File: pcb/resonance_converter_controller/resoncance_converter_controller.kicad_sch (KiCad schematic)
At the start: 53 parts, among them J2 USB_C_Receptacle_USB2.0_14P, J4 Conn_02x19_Odd_Even, J5 Conn_01x02, J6 FX18-120S-0.8SH, J7 Conn_ARM_SWD_TagConnect_TC2030, U22 USBLC6-2P6, U23 OPA356xxDBV, U24 AD5246BKSZ100-RL7

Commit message: Add io panel and fix controller pcb
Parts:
- added C101, C102: 100nF, Capacitor_SMD:C_0402_1005Metric, symbol Device:C
- added CN1: AXK5S40047YG, AXK5S40047YG:CONN-SMD_40P-P0.50_AXK5S40047YG, symbol AXK5S40047YG:AXK5S40047YG
- added J3: DF12NB_5.0_-20DP-0.5V_51_, DF12NB_5.0_-20DP-0.5V_51_:HRS_DF12NB_5.0_-20DP-0.5V_51_, symbol DF12NB_5.0_-20DP-0.5V_51_:DF12NB_5.0_-20DP-0.5V_51_
- added U25: TMUX1574RSV, Package_DFN_QFN:UQFN-16_1.8x2.6mm_P0.4mm, symbol Analog_Switch:TMUX1574RSV
- added U26: TMUX154ERSW, Package_DFN_QFN:UQFN-10_1.4x1.8mm_P0.4mm, symbol Analog_Switch:TMUX154ERSW
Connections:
- net ENCODER_CHA: now also U26.3 (A); no longer J6.80
- net ENCODER_CHB: now also U26.5 (B); no longer J6.19
- net GND: now also C101.2, C102.2, CN1.21, CN1.22, CN1.23, CN1.24, CN1.25, CN1.26, CN1.27, CN1.28, CN1.29, CN1.30, CN1.31, CN1.32, CN1.33, CN1.34, CN1.35, CN1.36, CN1.37, CN1.38, CN1.39, CN1.40, J3.16, J3.18, J3.20, U25.13 (~{EN}), U25.6 (GND), U26.4 (GND), U26.8 (~{EN}); no longer J4.13 (Pin_13), J6.60
- net HRTIM_EEV9: now also J3.5
- net INT_I2C_SCL: now also J3.8
- net INT_I2C_SDA: now also J3.10
- net LCD_DC: now also U25.5 (D2); no longer J6.20
- net LCD_MOSI: now also U25.7 (D3); no longer J6.90
- net LCD_SCK: now also U25.2 (D1); no longer J6.29
- net LCD_SS: now also U25.10 (D4); no longer J6.92
- net VCC: now also C101.1, C102.1, J3.2, U25.14 (VDD), U26.9 (VCC)
- net VOUT: now also CN1.10, CN1.12, CN1.14, CN1.16, CN1.18, CN1.2, CN1.20, CN1.4, CN1.6, CN1.8
- net VSYS: now also CN1.1, CN1.11, CN1.13, CN1.15, CN1.17, CN1.19, CN1.3, CN1.5, CN1.7, CN1.9
- net Controller/NRST renamed NRST
- net NRST: now also J3.1
- net Controller/SWCLK renamed SWCLK
- net SWCLK: now also J3.19
- net Controller/SWDIO renamed SWDIO
- net SWDIO: now also J3.17
- net Power supply/3.3VP renamed +3.3VP
- net +3.3VP: now also J3.4, J3.6
- new net AUX_ADC: J4.13 (Pin_13), J6.60
- new net KEY_INT: J3.3
- new net LOCAL_ENCODER: U26.10 (SEL)
- new net LOCAL_ENCODER_CHA: J3.14, U26.1 (A0)
- new net LOCAL_ENCODER_CHB: J3.15, U26.7 (B0)
- new net LOCAL_LCD: U25.15 (SEL)
- new net LOCAL_LCD_DC: J3.11, U25.3 (S2A)
- new net LOCAL_LCD_MOSI: J3.7, U25.9 (S3A)
- new net LOCAL_LCD_SCK: J3.13, U25.16 (S1A)
- new net LOCAL_LCD_SS: J3.9, U25.12 (S4A)
- new net REMOTE_ENCODER_CHA: J6.80, U26.2 (A1)
- new net REMOTE_ENCODER_CHB: J6.19, U26.6 (B1)
- new net REMOTE_LCD_DC: J6.20, U25.4 (S2B)
- new net REMOTE_LCD_MOSI: J6.90, U25.8 (S3B)
- new net REMOTE_LCD_SCK: J6.29, U25.1 (S1B)
- new net REMOTE_LCD_SS: J6.92, U25.11 (S4B)
- new net /QON: J3.12
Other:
- sheet Analog preprocess ports: added AUX_ADC, AUX_ADC_OUT; removed none
- sheet Controller ports: added AUX_ADC_OUT, KEY_INT, LCD_LOCAL, LOCAL_ENCODER; removed none
- sheet Power supply ports: added /QON; removed none

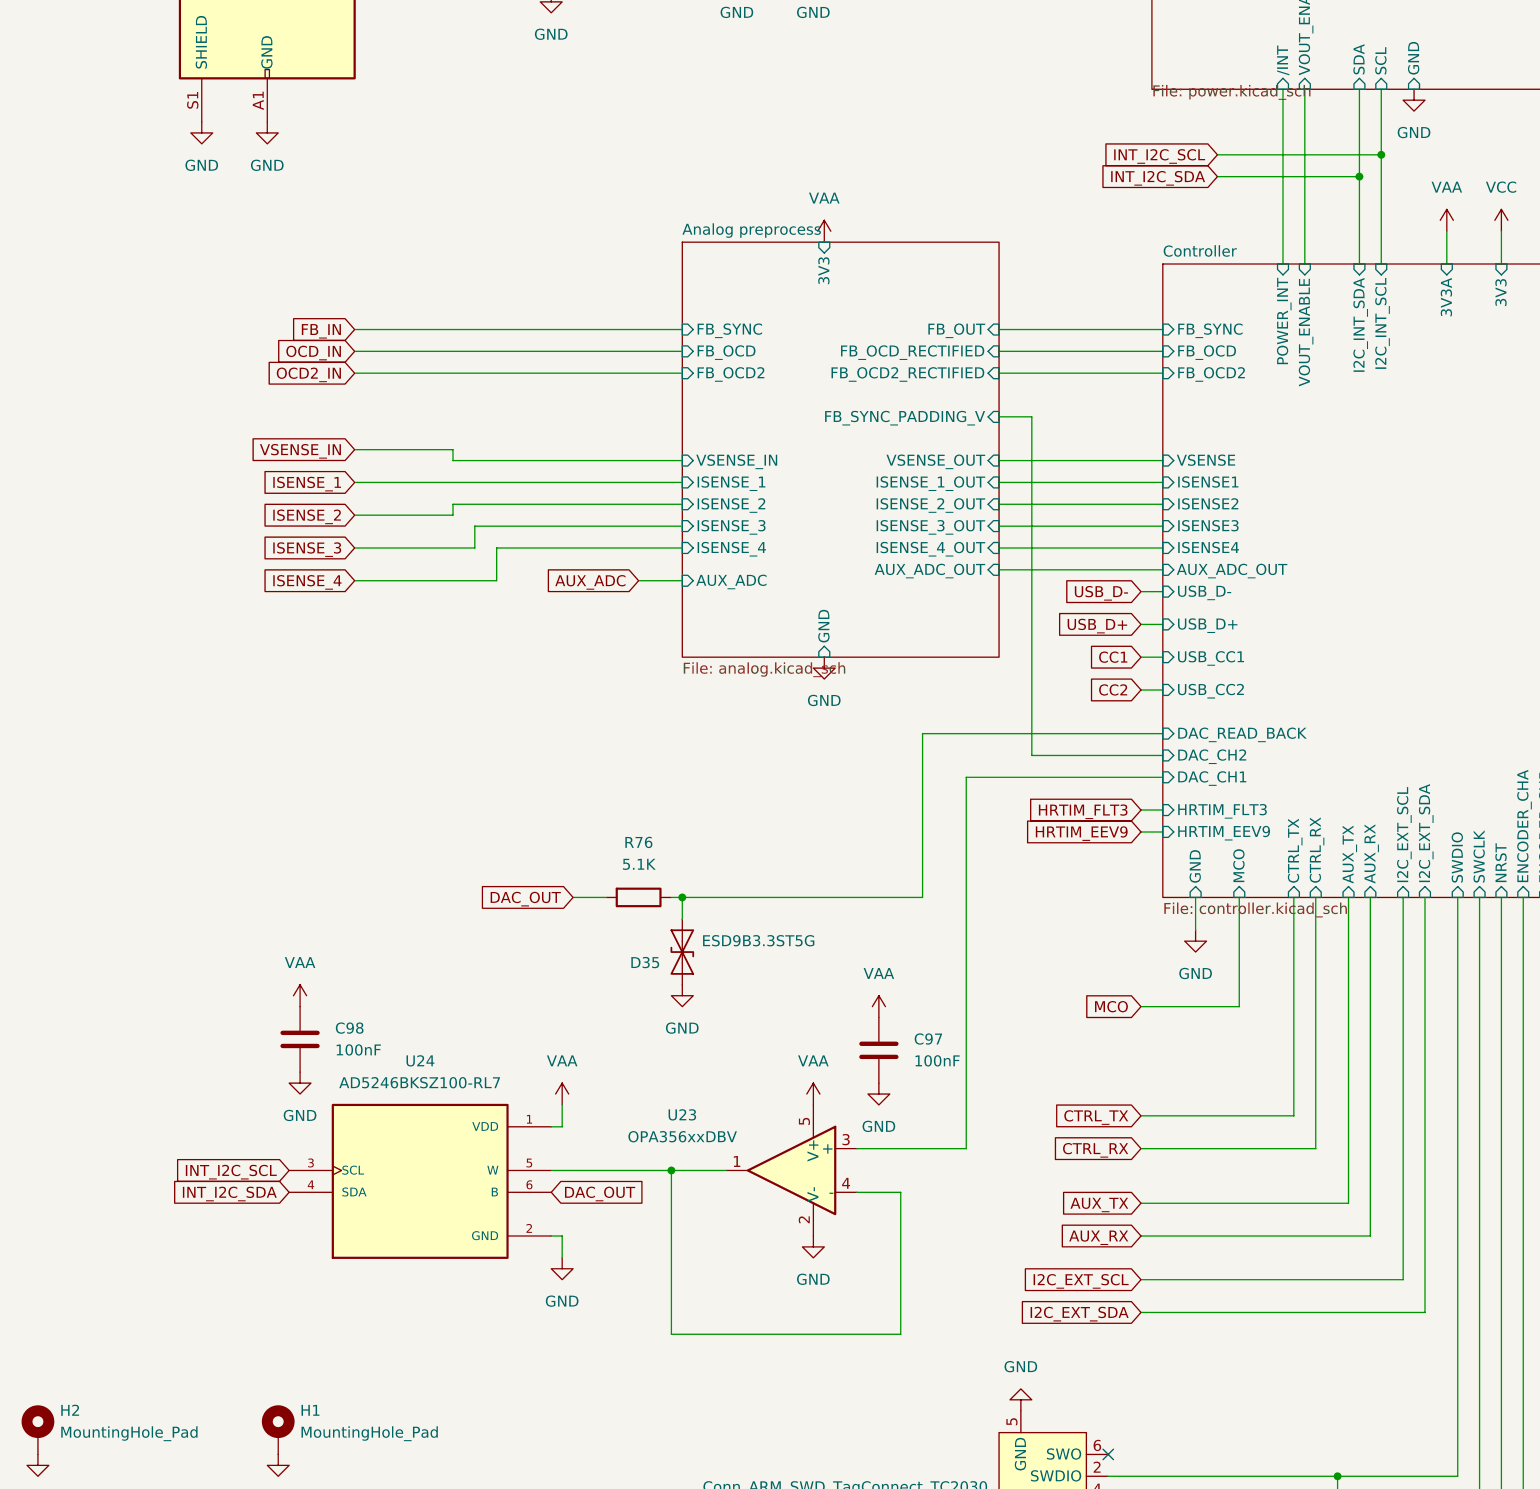
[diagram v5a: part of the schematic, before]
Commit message: Add digital pots to auto adjust gain
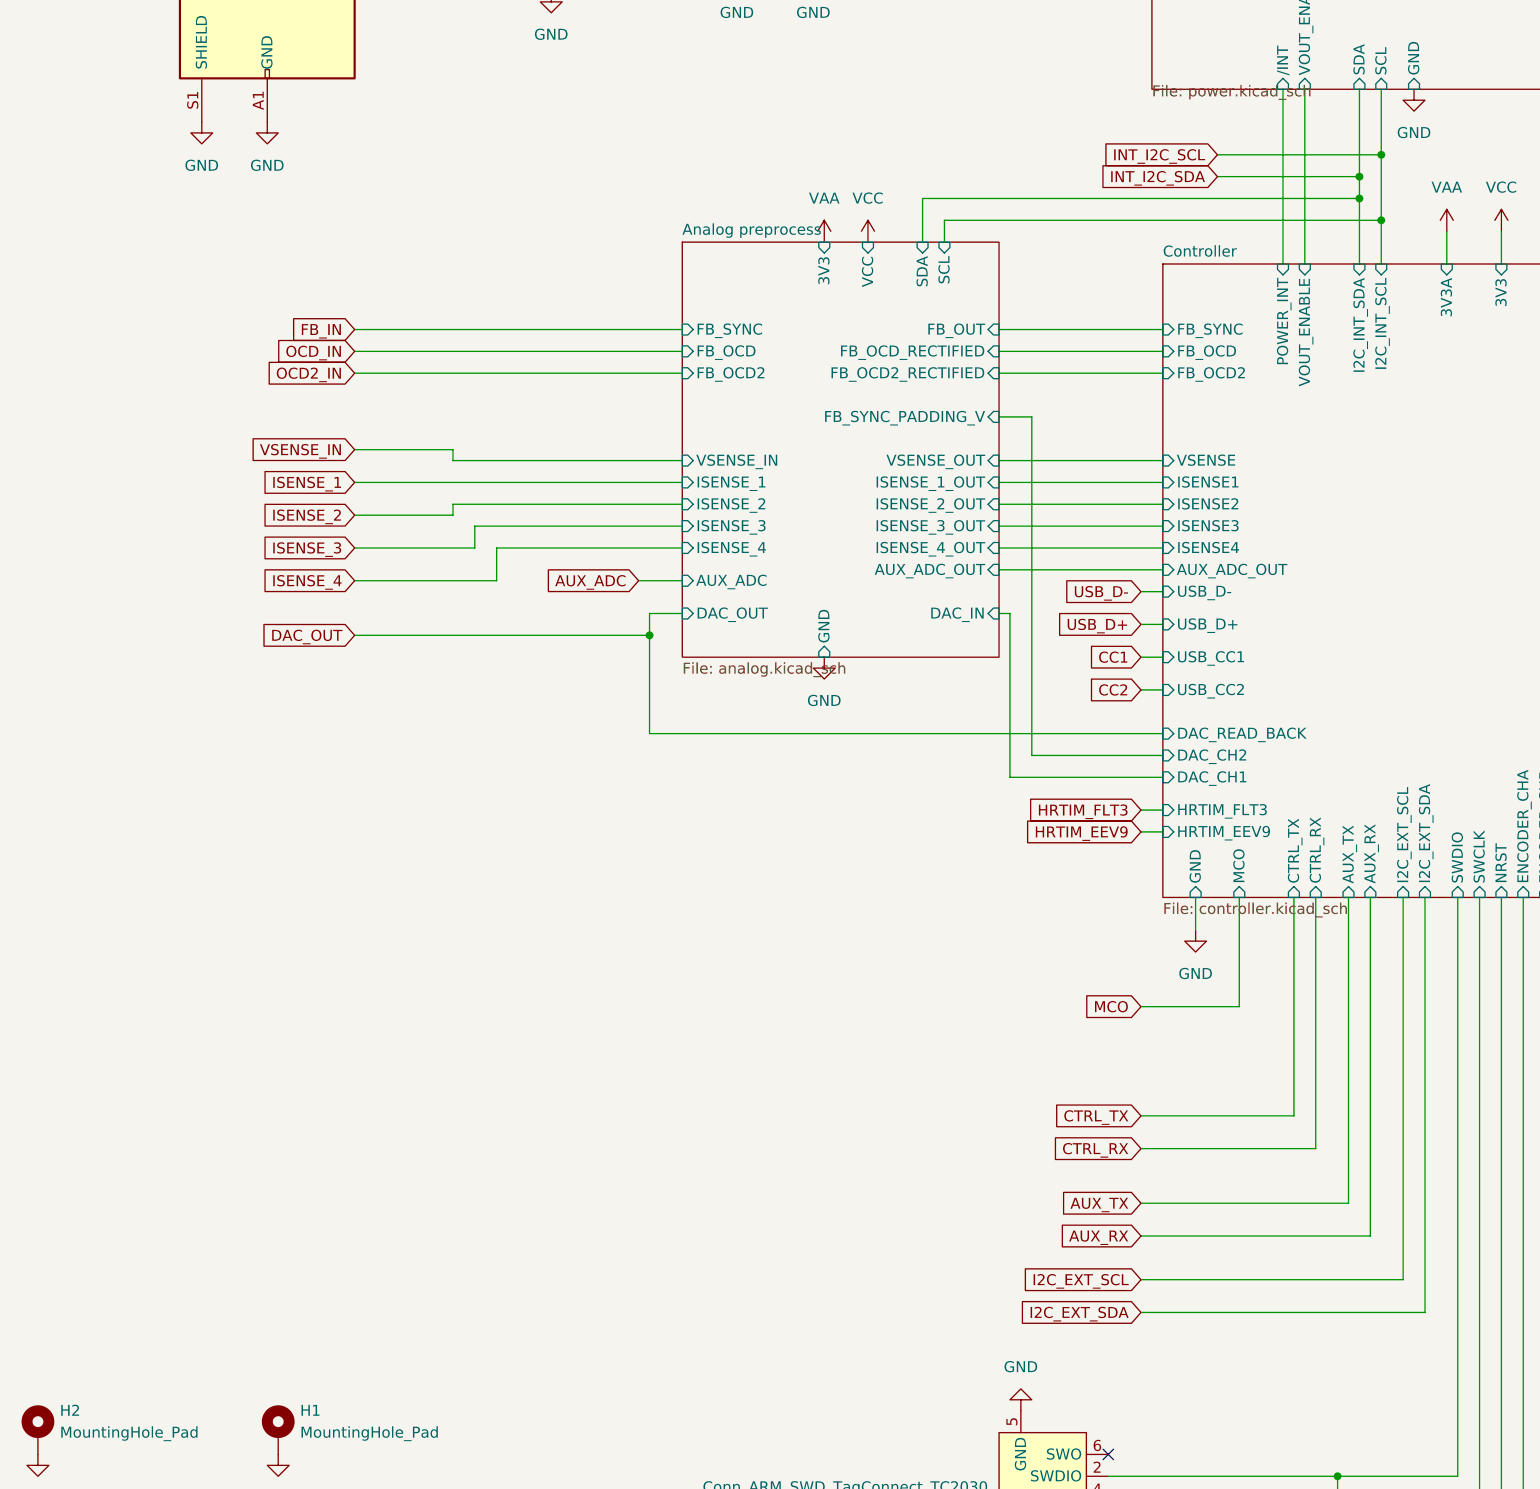
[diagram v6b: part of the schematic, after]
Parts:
- removed C97, C98: 100nF, Capacitor_SMD:C_0402_1005Metric, symbol Device:C
- removed D35: ESD9B3.3ST5G, Diode_SMD:D_SOD-923, symbol Diode:ESD9B3.3ST5G
- removed R76: 5.1K, Resistor_SMD:R_0402_1005Metric, symbol Device:R
- removed U23: OPA356xxDBV, Package_TO_SOT_SMD:SOT-23-5, symbol Amplifier_Operational:OPA356xxDBV
- removed U24: AD5246BKSZ100-RL7, AD5246BKSZ100-RL7:SOT65P210X110-6N, symbol AD5246BKSZ100-RL7:AD5246BKSZ100-RL7
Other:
- sheet Analog preprocess ports: added DAC_IN, DAC_OUT, SCL, SDA, VCC; removed none
